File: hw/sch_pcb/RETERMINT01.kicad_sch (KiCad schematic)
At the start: 72 parts, among them J1 Conn_02x05_Odd_Even, J10 RJ45_LED_Shielded, J11 HEADER_2x01_PARALLEL, J16 HEADER_2x01_PARALLEL, J2 Barrel_Jack_Switch, J3 MCX, J4 HEADER_2x01_PARALLEL, J5 HEADER_2x01_PARALLEL, J6 HEADER_2x05_PARALLEL, J7 Raspberry_Pi_4, J8 HEADER_2x01_PARALLEL, M1 HOLE, M2 HOLE, M3 HOLE, M4 HOLE, Q1 BC817-25, Q2 BC817-25, U1 USBLC6-2SC6, U2 MIC5504-3.3YM5, U3 NEO-M9N, U4 ADM2483xRW, U5 ADM2483xRW, U6 ADM2483xRW, U7 TPSM33606S5QRDNRQ1

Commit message: wip, layout
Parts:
- added JP2: SolderJumper_2_Open, Jumper:SolderJumper-2_P1.3mm_Open_RoundedPad1.0x1.5mm, symbol Jumper:SolderJumper_2_Open
- added R20, R21: 220R, Resistor_SMD:R_0805_2012Metric, symbol Device:R
- added TP1: GND_DIG, Connector_Pin:Pin_D1.4mm_L8.5mm_W2.8mm_FlatFork, symbol Connector:TestPoint
- added TP2: 24V, Connector_Pin:Pin_D1.4mm_L8.5mm_W2.8mm_FlatFork, symbol Connector:TestPoint
- added TP4: TestPoint, TestPoint:TestPoint_Pad_D1.5mm, symbol Connector:TestPoint
- C10: renamed from C7; footprint Mlab_R:SMD-0805 -> Capacitor_SMD:C_0805_2012Metric
- C11, C12: footprint (none) -> Capacitor_SMD:C_0805_2012Metric
- C2: renamed from C6; footprint (none) -> Capacitor_SMD:C_0805_2012Metric
- C3: renamed from C8; footprint (none) -> Capacitor_SMD:C_0805_2012Metric
- C4: renamed from C9; footprint (none) -> Capacitor_SMD:C_0805_2012Metric
- C5: renamed from C2; footprint Mlab_R:SMD-0805 -> Capacitor_SMD:C_0805_2012Metric
- C6: renamed from C5; footprint Mlab_R:SMD-0805 -> Capacitor_SMD:C_0805_2012Metric
- C7: renamed from C10; footprint Mlab_R:SMD-0805 -> Capacitor_SMD:C_0805_2012Metric
- C8: renamed from C3; footprint Mlab_R:SMD-0805 -> Capacitor_SMD:C_0805_2012Metric
- C9: renamed from C4; footprint Mlab_R:SMD-0805 -> Capacitor_SMD:C_0805_2012Metric
- D3, D6: footprint Mlab_D:LED_1206 -> LED_SMD:LED_1206_3216Metric
- D8: renamed from D10; footprint (none) -> Diode_SMD:D_SMC
- F1: renamed from F2; footprint (none) -> Fuse:Fuse_0805_2012Metric
- F2: renamed from F1; value Fuse_Small -> 1A; footprint (none) -> Fuse:Fuse_0805_2012Metric
- J2: footprint (none) -> Connector_BarrelJack:BarrelJack_Horizontal; now not fitted; now left out of the parts list
- J8: renamed from J3; value MCX -> u.fl
- M1, M2, M3, M4: now left out of the parts list
- NT1: renamed from NT2; footprint (none) -> NetTie:NetTie-2_SMD_Pad0.5mm
- R1: footprint Mlab_R:SMD-0805 -> Resistor_SMD:R_0805_2012Metric
- R10: renamed from R6; footprint Mlab_R:SMD-0805 -> Resistor_SMD:R_0805_2012Metric
- R11: renamed from R7; footprint Mlab_R:SMD-0805 -> Resistor_SMD:R_0805_2012Metric
- R12: renamed from R8; footprint Mlab_R:SMD-0805 -> Resistor_SMD:R_0805_2012Metric
- R13: renamed from R9; footprint Mlab_R:SMD-0805 -> Resistor_SMD:R_0805_2012Metric
- R14: renamed from R11; footprint Mlab_R:SMD-0805 -> Resistor_SMD:R_0805_2012Metric
- R15: renamed from R21; footprint Mlab_R:SMD-0805 -> Resistor_SMD:R_0805_2012Metric
- R16: renamed from R15; footprint Mlab_R:SMD-0805 -> Resistor_SMD:R_0805_2012Metric
- R17: renamed from R10; footprint Mlab_R:SMD-0805 -> Resistor_SMD:R_0805_2012Metric
- R18: renamed from R14; footprint Mlab_R:SMD-0805 -> Resistor_SMD:R_0805_2012Metric
- R19: renamed from R16; footprint Mlab_R:SMD-0805 -> Resistor_SMD:R_0805_2012Metric
- R2: renamed from R17; footprint Mlab_R:SMD-0805 -> Resistor_SMD:R_0805_2012Metric
- R3: renamed from R18; footprint Mlab_R:SMD-0805 -> Resistor_SMD:R_0805_2012Metric
- R4: renamed from R2; footprint Mlab_R:SMD-0805 -> Resistor_SMD:R_0805_2012Metric
- R5: renamed from R3; footprint Mlab_R:SMD-0805 -> Resistor_SMD:R_0805_2012Metric
- R6: renamed from R12; footprint Mlab_R:SMD-0805 -> Resistor_SMD:R_0805_2012Metric
- R7: renamed from R13; footprint Mlab_R:SMD-0805 -> Resistor_SMD:R_0805_2012Metric
- R8: renamed from R4; footprint Mlab_R:SMD-0805 -> Resistor_SMD:R_0805_2012Metric
- R9: renamed from R5; footprint Mlab_R:SMD-0805 -> Resistor_SMD:R_0805_2012Metric
- TP3: renamed from TP1; footprint (none) -> TestPoint:TestPoint_Pad_D1.5mm; now left out of the parts list
- renumbered D7 to D5, D5 to D7, J7 to J10, J10 to J11, J6 to J3, J11 to J6, J16 to J7, J8 to J9, JP2 to JP3, Q2 to Q1, Q1 to Q2, U7 to U1, U1 to U2, U2 to U3, U3 to U4, U4 to U5, U5 to U6, U6 to U7
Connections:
- net GND is gone; now on net GND_DIG: M1.1, M2.1, M3.1, M4.1
- net +24V_IN: now also TP2.1
- net +3V3: now also JP1.3 (B)
- net +3V3_GPS: now also D3.2 (A)
- net +5V_OUT: now also R20.1
- net GNDPWR: now also TP1.1
- net GND_DIG: now also JP2.2 (B)
- net GND_GPS: now also JP2.1 (A)
- net GND_OUT: now also J11.11, J11.9, J11.SH
- net at C8.1, C9.1, JP1.1 (A)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: no longer D3.2 (A)
- net at J11.10: now also R20.2
- net at J11.12: now also R21.2
- new net: R21.1, TP4.1
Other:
- moved on the sheet: D3, JP1, NT1, R17

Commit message: PS1 default-off: add pull-up on Q1 base, rework R2/R3
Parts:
- added R20, R21, R23: 220R, Resistor_SMD:R_0805_2012Metric, symbol Device:R
- added R3: 10k, Resistor_SMD:R_0805_2012Metric, symbol GPS02A-rescue:R-Device
- R2: value 10k -> 1k
- R4: renamed from R3; value 100k -> 10k; now not fitted
- renumbered R9 to R10, R10 to R11, R11 to R12, R12 to R13, R13 to R14, R14 to R15, R15 to R16, R16 to R17, R17 to R18, R18 to R19, R19 to R22, R20 to R24, R21 to R25, R4 to R5, R5 to R6, R6 to R7, R7 to R8, R8 to R9
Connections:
- net +3V3: now also R3.1
- net 1A: now also R21.1
- net 1B: now also R21.2
- net 2A: now also R20.1
- net 2B: now also R20.2
- net 3A: now also R23.1
- net 3B: now also R23.2
- net TRIM: now reaches PS1.4 (COMMON), R7.2, R8.1
- net at Q1.1 (B), R2.2, R4.1: now also R3.2
- net PWR_OFF renamed PWR_ON
- no-connect marks 14 -> 39
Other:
- moved on the sheet: R2

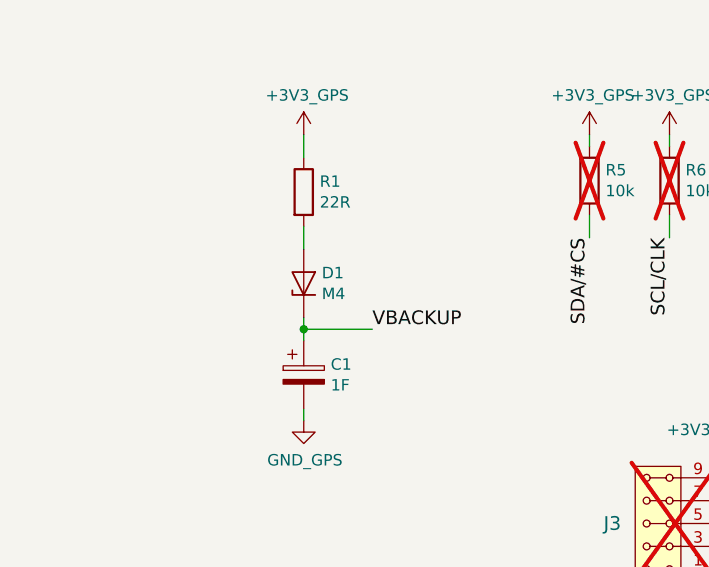
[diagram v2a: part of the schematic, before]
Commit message: Fix D1 symbol type, fill title block
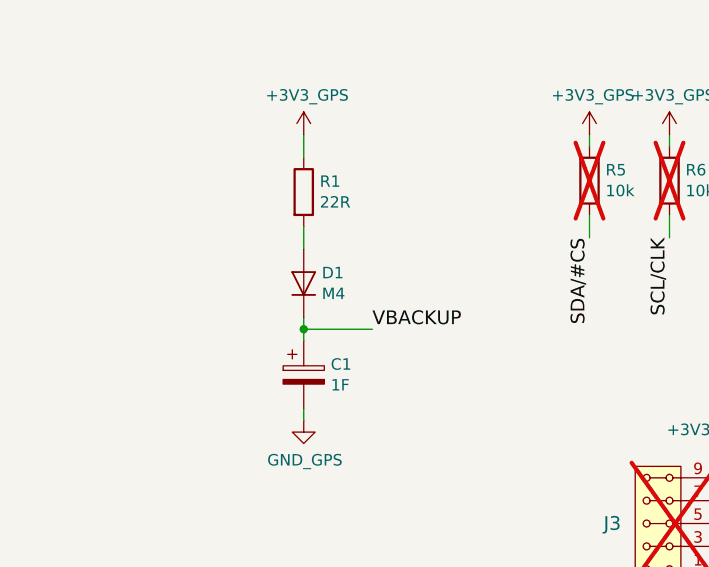
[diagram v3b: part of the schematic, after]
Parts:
- D1: symbol GPS02A-rescue:D_Zener-Device -> GPS02A-rescue:D-Device
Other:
- company: (none) -> MLAB
- title: (none) -> RETERMINT01 – RETERMINAL DM Interface Board
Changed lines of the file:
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@@
 	(generator_version "9.0")
 	(paper "A3")
+	(title_block
+		(title "RETERMINT01 – RETERMINAL DM Interface Board")
+		(date "2026-05-18")
+		(rev "A")
+		(company "MLAB")
+	)
 	(text "Propojeni s hrebinkem pomoci tohoto: https://mou.sr/4wiD7Ls nebo ekvivalentu. "
 		(exclude_from_sim no)
@@
 	)
 	(symbol
-		(lib_id "GPS02A-rescue:D_Zener-Device")
+		(lib_id "GPS02A-rescue:D-Device")
 		(at 26.67 83.82 90)
 		(unit 1)

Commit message: Update DC/DC label
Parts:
- PS1: value THN_30-2423WI -> THN-30-2415WIR; Manufacturer_Part_Number THN 30-2423WI -> THN-30-2415WIR; Mouser Part Number 495-THN30-2423WI -> 495-THN30-2415WIR
